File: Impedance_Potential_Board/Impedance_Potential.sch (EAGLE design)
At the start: 39 parts, among them IC1 MAX30001GCWV+, U4 AP2112K-1.8V

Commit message: MAX30001G
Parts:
- removed SJ4: LED DISABLE, SparkFun-Jumpers:JUMPER-SMT_2_NC_TRACE_NO-SILK
- added AOUT, BIN, BIP, DRVN, DRVP, ECGN, ECGP: TEST-POINT3, SparkFun-Connectors:TEST-POINT3
- added BP_BN, DN_BN, DP_BP, EC_UNBAL, EN_BN, EN_UNBAL, EP_BP, EP_EN, EP_UNBAL, RBN, RBP: JUMPER-SMT_2_NO_SILK, SparkFun-Jumpers:JUMPER-SMT_2_NO_SILK
- added C21: 10uF, SparkFun-Capacitors:10UF-0603-6.3V-20%
- added C22, C23, C24: 47nF, SparkFun-Capacitors:47NF-0603-25V-5%
- added D2, D3, D4, D5, D6, D7, D8: ESD7551N2T5G, ESD7551N2T5G:ESD7551N2T5G
- added ECGC: ECGC, SparkFun-Connectors:TEST-POINT3
- added FCLK: FCLK, SparkFun-Connectors:TEST-POINT3
- added J1: (no value), SparkFun-Connectors:CONN_08"
- added LED_ENABLE: LED ENABLE, SparkFun-Jumpers:JUMPER-SMT_2_NC_PASTE_SILK
- added P_DWN_ENABLE, P_UP_ENABLE: JUMPER-SMT_2_NC_PASTE_SILK, SparkFun-Jumpers:JUMPER-SMT_2_NC_PASTE_SILK
- added R11, R12, R13, R14, R15, R17: 100k, SparkFun-Resistors:100KOHM-0603-1/10W-1%
- added R18: 100, SparkFun-Resistors:100OHM-0603-1/4W-5%
- C1, C2: value 47nF -> 0.22uF; device SparkFun-Capacitors:47NF-0603-25V-5% -> SparkFun-Capacitors:0.22UF-0603-25V-10%
- C11, C13, C17: device rcl:C-EUC0603 -> SparkFun-Capacitors:0.1UF-0603-25V-(+80/-20%)
- C12, C14, C19, C20: device rcl:C-EUC0603 -> SparkFun-Capacitors:10UF-0603-6.3V-20%
- R1, R2, R3: value 200k -> 47k; device SparkFun-Resistors:200KOHM-0603-1/10W-1% -> SparkFun-Resistors:47KOHM-0603-1/10W-1%
- R10, R5, R6, R7, R8, R9: value 10M -> 10; device SparkFun-Resistors:10MOHM-0603-1/10W-5% -> SparkFun-Resistors:10OHM-0603-1/10W-1%
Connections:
- net N$10 renamed CAPP
- net N$11 renamed CAPN
- net N$12 renamed VREF
- net N$16 renamed VBG
- net N$17 renamed RBIAS
- net N$18 renamed CSB_
- net N$2 renamed DRVP_
- net N$20 renamed CPLL
- net N$21 renamed SCLK_
- net N$22 renamed SDI_
- net N$23 renamed SDO_
- net N$24 renamed INT2B_
- net N$25 renamed INTB_
- net N$4 renamed DRVN_
- removed net N$1: C1.2, DRV.2
- removed net N$13: C3.1, C5.1, IC1.BIN, IMPEDANCE.3
- removed net N$14: ECG.3, R2.2
- removed net N$15: C7.2, C8.2, IC1.ECGN, R2.1
- removed net N$19: C11.1, C12.1, C15.2, C17.1, IC1.AVDD, IC1.DVDD, U4.OUT
- removed net N$27: IC1.FCLK
- removed net N$3: ECG.2, R1.2
- removed net N$5: C2.2, DRV.3
- removed net N$6: C4.2, C5.2, IC1.BIP, IMPEDANCE.2
- removed net N$7: ECG.1, R3.2
- removed net N$8: C20.1, IC1.VCM, R3.1
- removed net N$9: C6.1, C8.1, IC1.ECGP, R1.1
- removed net VDD: C13.1, C14.1, C16.2, IC1.OVDD, U4.EN, U4.IN
- new net 1.8V: C11.1, C12.1, C15.2, C17.1, C21.1, IC1.AVDD, IC1.DVDD, U4.OUT
- new net AOUT: AOUT.1, IC1.N.C.
- new net BIN: BIN.1, BP_BN.2, C3.1, C5.1, D4.1, DN_BN.1, EN_BN.2, IC1.BIN, IMPEDANCE.3, RBN.2
- new net BIP: BIP.1, BP_BN.1, C4.2, C5.2, D5.1, DP_BP.1, EP_BP.2, IC1.BIP, IMPEDANCE.2, RBP.1
- new net CSB: J1.1, R10.1, R15.2
- new net DRVN: C2.2, D3.1, DN_BN.2, DRV.3, DRVN.1
- new net DRVP: C1.2, D2.1, DP_BP.2, DRV.2, DRVP.1
- new net ECGC: C24.2, D6.2, ECG.1, ECGC.1, EC_UNBAL.1, R3.2
- new net ECGN: C23.2, D8.2, ECG.3, ECGN.1, EN_BN.1, EN_UNBAL.1, R2.2
- new net ECGN_: C23.1, C7.2, C8.2, EN_UNBAL.2, EP_EN.1, IC1.ECGN, R2.1
- new net ECGP: C22.2, D7.2, ECG.2, ECGP.1, EP_BP.1, EP_UNBAL.1, R1.2
- new net ECGP_: C22.1, C6.1, C8.1, EP_EN.2, EP_UNBAL.2, IC1.ECGP, R1.1
- new net FCLK_: FCLK.1, IC1.FCLK
- new net INT1B: J1.6, R14.2, R5.1
- new net INT2B: J1.5, R17.2, R6.1
- new net N$29: P_DWN_ENABLE.2, R11.1, R12.1, R13.1
- new net N$30: P_UP_ENABLE.2, R14.1, R15.1, R17.1
- new net N$32: R18.2, RBN.1
- new net N$33: R18.1, RBP.2
- new net SCLK: J1.2, R13.2, R9.1
- new net SDI: J1.3, R11.2, R8.1
- new net SDO: J1.4, R12.2, R7.1
- new net VCM: C20.1, C24.1, EC_UNBAL.2, IC1.VCM, R3.1
- net 3.3V: now also C13.1, C14.1, C16.2, IC1.OVDD, J1.7, P_UP_ENABLE.1, U4.EN, U4.IN
- net GND: now also C21.2, D2.2, D3.2, D4.2, D5.2, D6.1, D7.1, D8.1, J1.8, LED_ENABLE.1, P_DWN_ENABLE.1; no longer SJ4.1
- net N$28: now also LED_ENABLE.2; no longer SJ4.2
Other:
- note added: "1.8V to AVDD and DVDD 3.3V to OVDD"
- note added: "2 Electrode ECG & Respiration: DRVP-ECGP DRVN-ECGN BIN-ECGN BIP-ECGP"
- note added: "4 Electrode ECG & Respiration: BIN-ECGN BIP-ECGP"
- note added: "BIOZ with 100Ohm Test: RBN-RBP DRVP-BIP DRVN-BIN"
- note added: "Default BioZ Frequency: FMSTR/64 = 500Hz To measure 100 Ohm: increase frequency or change internal lower filter cut off."
- note added: "ECG , R-to-T, BioZ Signals: DRVP-BIP DRVN-BIN RBP and RBN EN_UNBAL and EP_UNBAL and EC_UNBAL"
- note added: "Galvanic Skin Response: DRVN-BIN DRVP-BIP 125, 250 or 500Hz 220nF blocking filter on DRVP/N"
- note added: "Urs Utzinger"
- moved on the sheet: C1, C10, C11, C12, C13, C14, C15, C16, C17, C18, C19, C2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

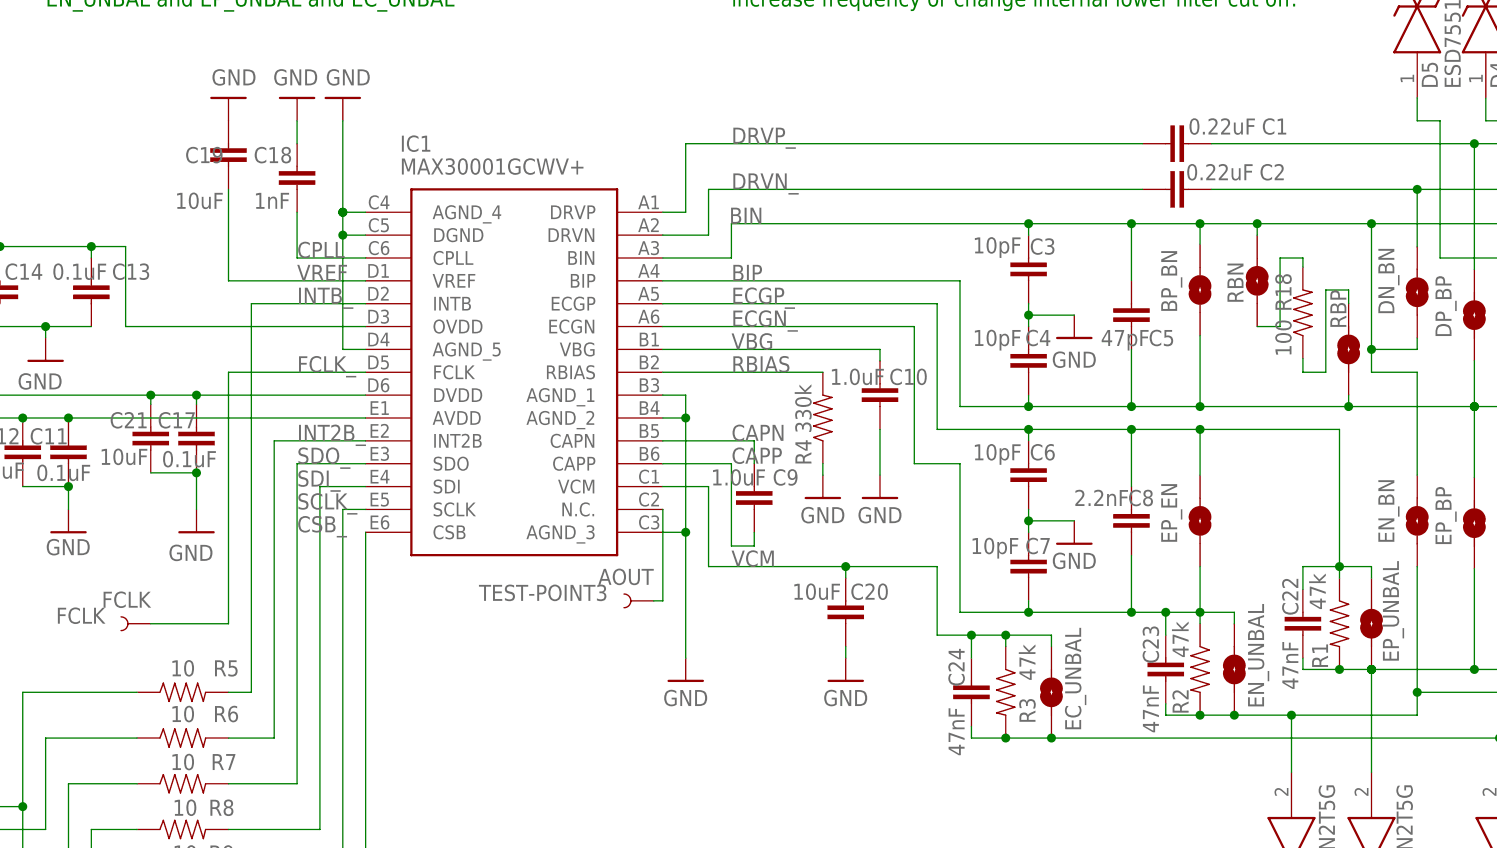
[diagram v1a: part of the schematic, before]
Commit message: BOM MAX30001G and board updates
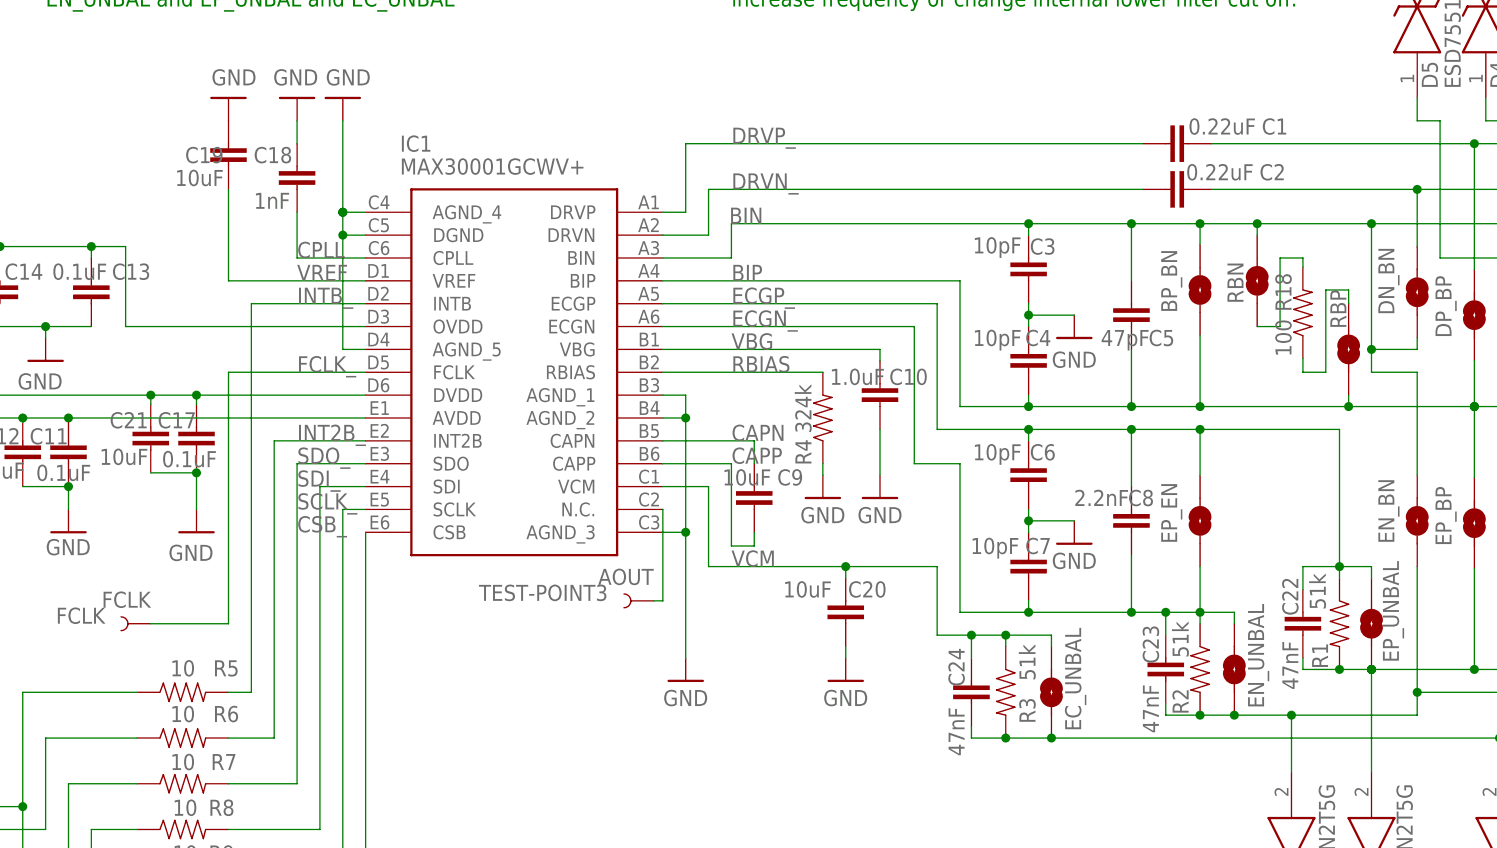
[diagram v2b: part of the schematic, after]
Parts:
- C9: value 1.0uF -> 10uF; device SparkFun-Capacitors:1.0UF-0603-16V-10% -> SparkFun-Capacitors:10UF-0603-6.3V-20%
- R1, R2, R3: value 47k -> 51k
- R4: value 330k -> 324k

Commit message: CAM Impedance_Potential Board
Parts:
- added R19, R20, R21, R22, R23: 0, SparkFun-Resistors:0OHM-0603-1/10W-5%
- J1: value (none) -> Header
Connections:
- new net N$1: C23.1, EN_UNBAL.2, R2.1, R22.2
- new net N$2: C24.1, EC_UNBAL.2, R23.2, R3.1
- new net N$3: C22.1, EP_UNBAL.2, R1.1, R21.2
- new net N$4: BP_BN.2, C3.1, C5.1, IC1.BIN, R19.1
- new net N$5: BP_BN.1, C4.2, C5.2, IC1.BIP, R20.1
- net BIN: now also R19.2; no longer BP_BN.2, C3.1, C5.1, IC1.BIN
- net BIP: now also R20.2; no longer BP_BN.1, C4.2, C5.2, IC1.BIP
- net ECGN_: now also R22.1; no longer C23.1, EN_UNBAL.2, R2.1
- net ECGP_: now also R21.1; no longer C22.1, EP_UNBAL.2, R1.1
- net VCM: now also R23.1; no longer C24.1, EC_UNBAL.2, R3.1
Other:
- moved on the sheet: AOUT, BP_BN, C1, C10, C11, C12, C13, C14, C15, C16, C17, C18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

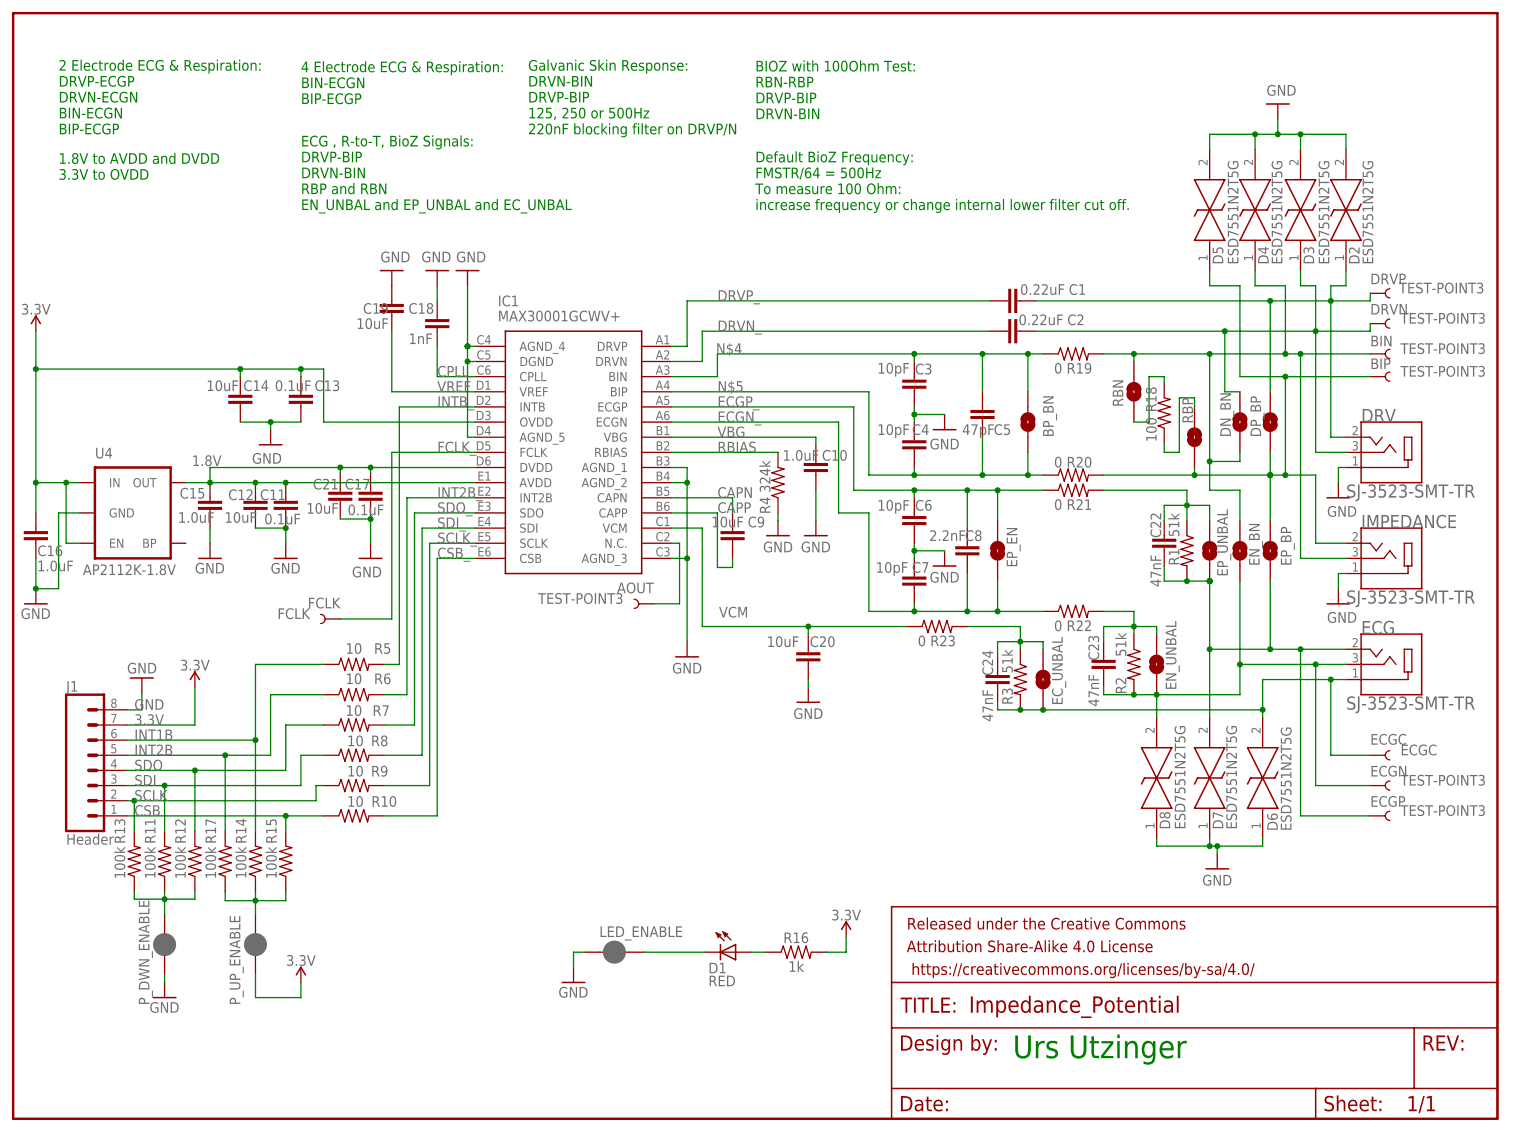
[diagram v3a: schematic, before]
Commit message: Board Updates
All LEDs at same location
Separated analog and digital ground
Updated impedance components
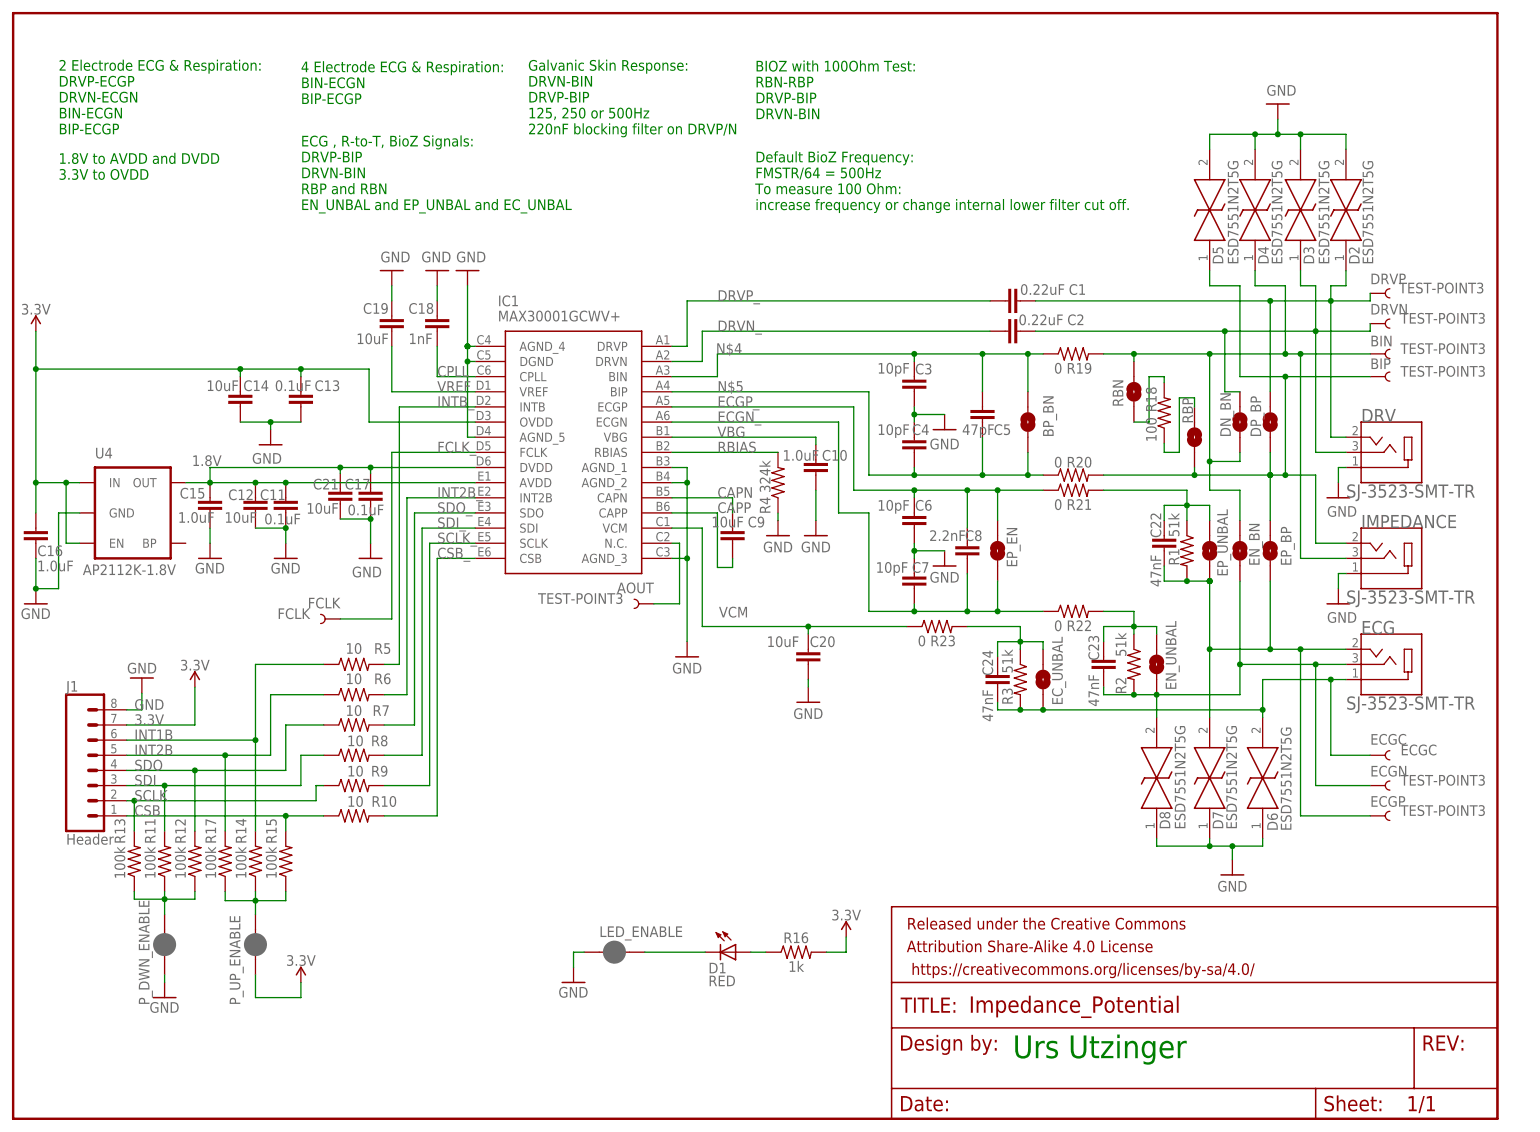
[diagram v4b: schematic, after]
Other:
- moved on the sheet: C19
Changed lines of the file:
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@@
 <attribute name="VALUE" x="-54.102" y="30.861" size="1.778" layer="96" rot="MR0"/>
 </instance>
-<instance part="C19" gate="G$1" x="-60.96" y="35.56" smashed="yes" rot="MR0">
+<instance part="C19" gate="G$1" x="-60.96" y="33.02" smashed="yes" rot="MR0">
 <attribute name="NAME" x="-61.468" y="35.941" size="1.778" layer="95" rot="MR0"/>
-<attribute name="VALUE" x="-61.468" y="33.401" size="1.778" layer="96" rot="MR0"/>
+<attribute name="VALUE" x="-61.468" y="30.861" size="1.778" layer="96" rot="MR0"/>
 </instance>
 <instance part="SUPPLY7" gate="1" x="-60.96" y="43.18" smashed="yes" rot="MR180">
@@
 <attribute name="VALUE" x="80.772" y="-50.546" size="1.778" layer="96" rot="R90"/>
 </instance>
-<instance part="SUPPLY11" gate="G$1" x="77.47" y="-57.15" smashed="yes" rot="MR0">
-<attribute name="VALUE" x="77.47" y="-59.055" size="1.778" layer="96" rot="MR0" align="center"/>
+<instance part="SUPPLY11" gate="G$1" x="80.01" y="-58.166" smashed="yes" rot="MR0">
+<attribute name="VALUE" x="80.01" y="-60.071" size="1.778" layer="96" rot="MR0" align="center"/>
 </instance>
 <instance part="DRVP" gate="G$1" x="103.124" y="39.37" smashed="yes">
@@
 <pinref part="D7" gate="G$1" pin="1"/>
 <wire x1="76.2" y1="-52.07" x2="76.2" y2="-53.34" width="0.1524" layer="91"/>
-<wire x1="76.2" y1="-53.34" x2="77.47" y2="-53.34" width="0.1524" layer="91"/>
-<wire x1="77.47" y1="-53.34" x2="85.09" y2="-53.34" width="0.1524" layer="91"/>
-<junction x="77.47" y="-53.34"/>
+<wire x1="76.2" y1="-53.34" x2="80.01" y2="-53.34" width="0.1524" layer="91"/>
+<wire x1="80.01" y1="-53.34" x2="85.09" y2="-53.34" width="0.1524" layer="91"/>
+<junction x="80.01" y="-53.34"/>
 <pinref part="D6" gate="G$1" pin="1"/>
 <wire x1="85.09" y1="-53.34" x2="85.09" y2="-52.07" width="0.1524" layer="91"/>
 <pinref part="SUPPLY11" gate="G$1" pin="GND"/>
-<wire x1="77.47" y1="-54.61" x2="77.47" y2="-53.34" width="0.1524" layer="91"/>
+<wire x1="80.01" y1="-55.626" x2="80.01" y2="-53.34" width="0.1524" layer="91"/>
 <wire x1="76.2" y1="-53.34" x2="67.31" y2="-53.34" width="0.1524" layer="91"/>
 <junction x="76.2" y="-53.34"/>
@@
 <pinref part="C19" gate="G$1" pin="1"/>
 <pinref part="SUPPLY7" gate="1" pin="GND"/>
+<wire x1="-60.96" y1="38.1" x2="-60.96" y2="40.64" width="0.1524" layer="91"/>
 </segment>
 <segment>
@@
 <pinref part="C19" gate="G$1" pin="2"/>
 <wire x1="-46.99" y1="22.86" x2="-60.96" y2="22.86" width="0.1524" layer="91"/>
-<wire x1="-60.96" y1="22.86" x2="-60.96" y2="33.02" width="0.1524" layer="91"/>
+<wire x1="-60.96" y1="22.86" x2="-60.96" y2="30.48" width="0.1524" layer="91"/>
 <label x="-53.34" y="22.86" size="1.778" layer="95"/>
 </segment>
@@
 <wire x1="-76.2" y1="26.67" x2="-86.36" y2="26.67" width="0.1524" layer="91"/>
 <junction x="-76.2" y="26.67"/>
-<wire x1="-76.2" y1="26.67" x2="-72.39" y2="26.67" width="0.1524" layer="91"/>
-<wire x1="-72.39" y1="17.78" x2="-72.39" y2="26.67" width="0.1524" layer="91"/>
+<wire x1="-76.2" y1="26.67" x2="-64.77" y2="26.67" width="0.1524" layer="91"/>
+<wire x1="-64.77" y1="17.78" x2="-64.77" y2="26.67" width="0.1524" layer="91"/>
 <pinref part="IC1" gate="G$1" pin="OVDD"/>
-<wire x1="-46.99" y1="17.78" x2="-72.39" y2="17.78" width="0.1524" layer="91"/>
+<wire x1="-46.99" y1="17.78" x2="-64.77" y2="17.78" width="0.1524" layer="91"/>
 <wire x1="-86.36" y1="26.67" x2="-120.65" y2="26.67" width="0.1524" layer="91"/>
 <junction x="-86.36" y="26.67"/>
